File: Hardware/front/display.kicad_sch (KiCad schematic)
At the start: 8 parts

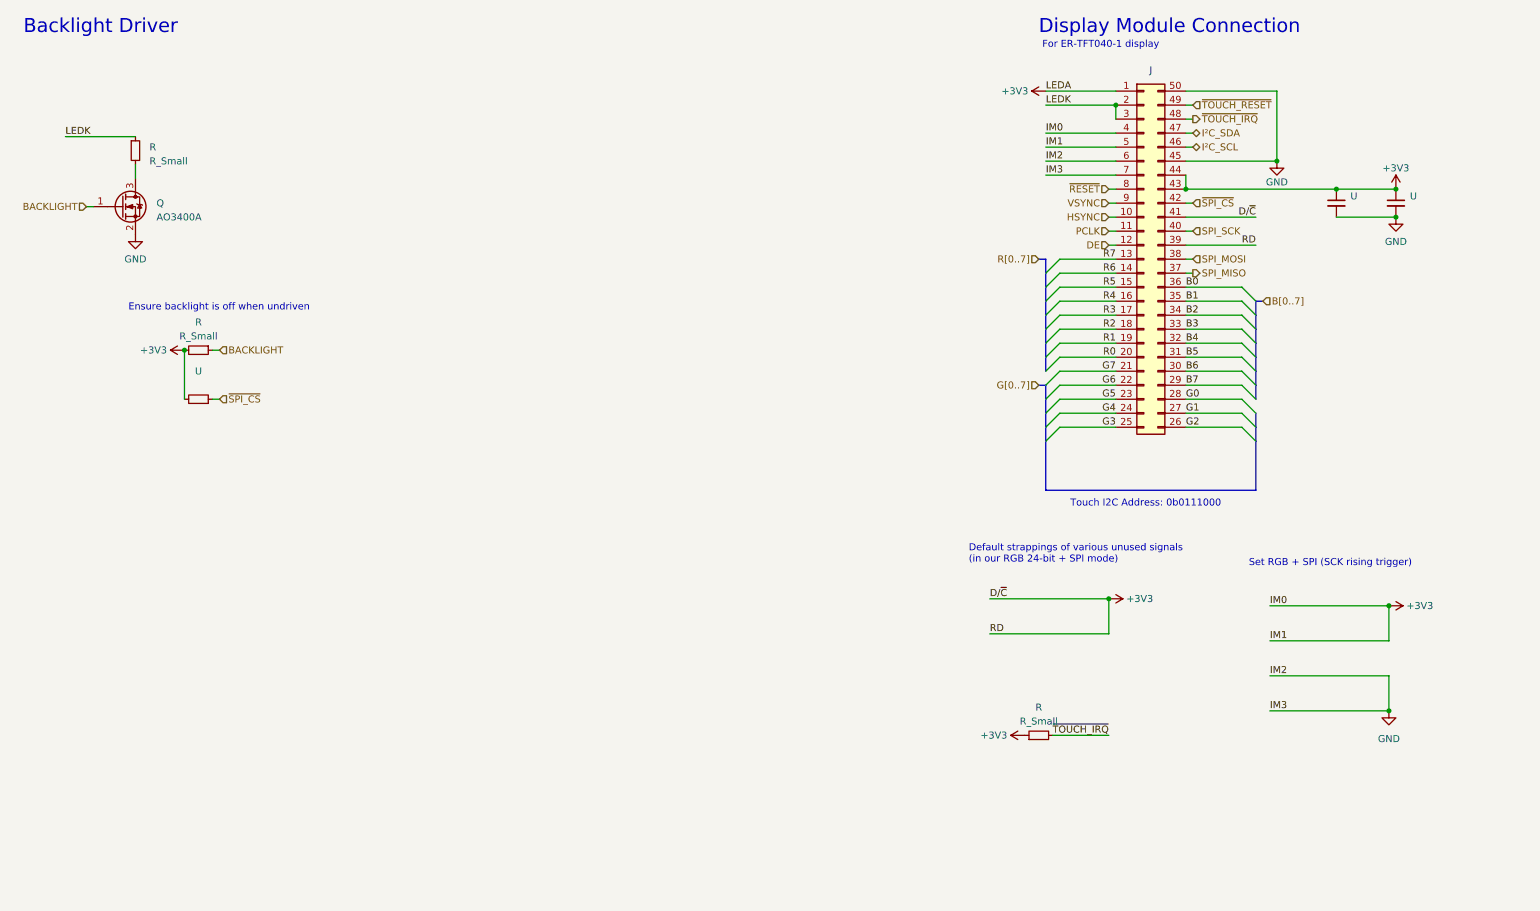
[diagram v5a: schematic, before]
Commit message: hw: First pass at new front panel
- Finished routing all signals on the front panel

- Put back the LED controller (PCA9955B) since that's a very nice and
  convenient way to drive the LEDs; it's driven via a "private" I2C bus
  from the RP2040 instead of the host controlling it.

  The touch panel controller is also hanging off this private bus so we
  can deal with it.

- Made trigger LED bicolor (green/orange)
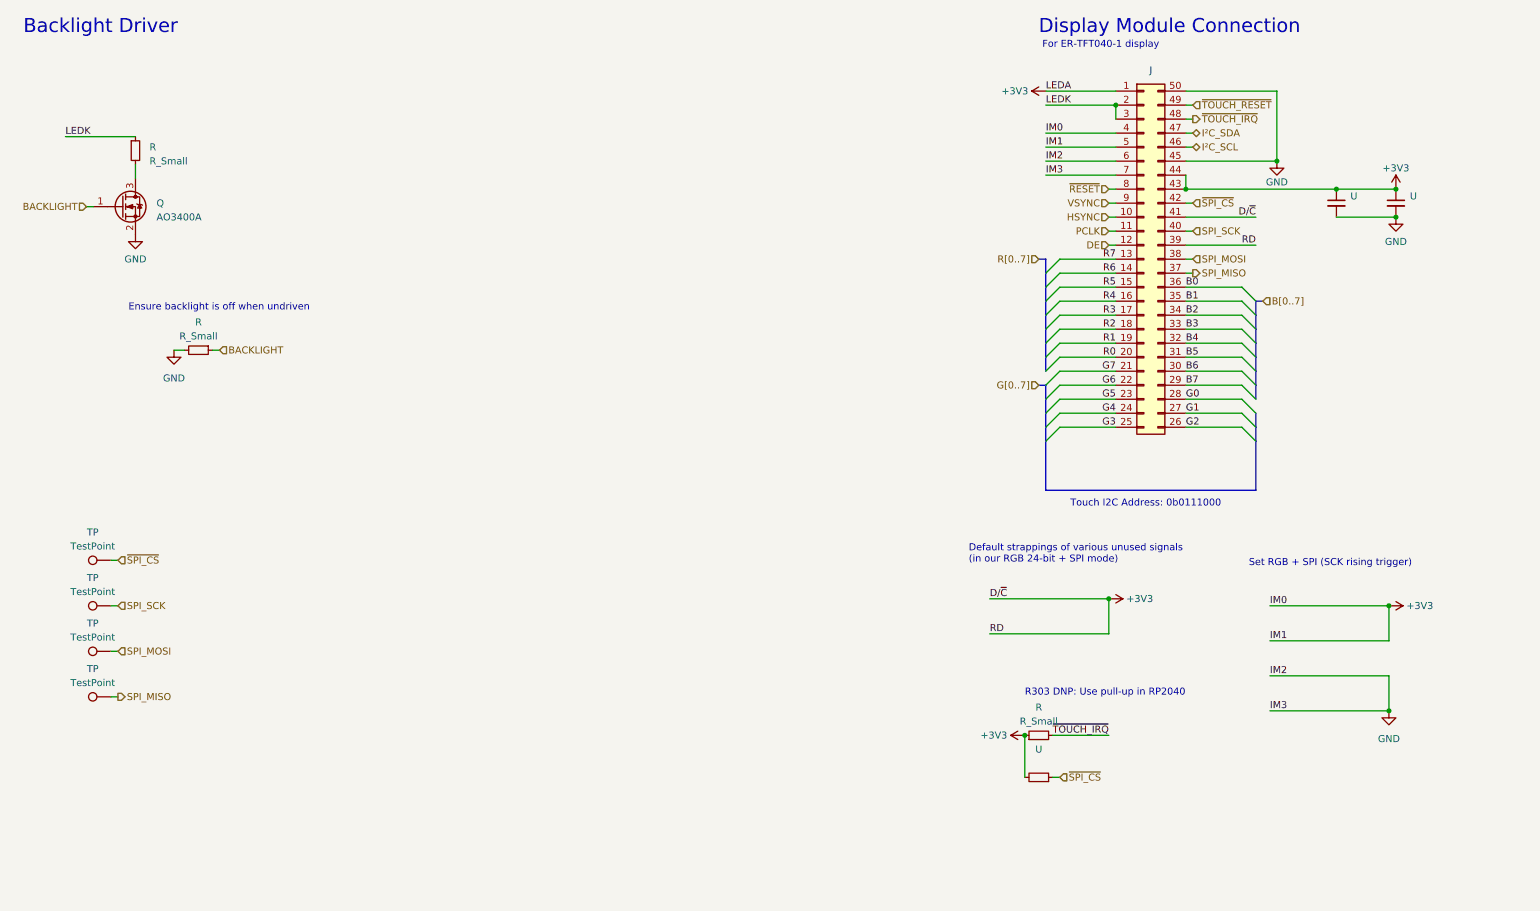
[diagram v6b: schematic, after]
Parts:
- added TP (x4): TestPoint, symbol Connector:TestPoint
- R: now left out of the parts list
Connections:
- net +3V3: no longer R.2
- net GND: now also R.2
- net SPI_MISO: now also TP.1
- net SPI_MOSI: now also TP.1
- net SPI_SCK: now also TP.1
- net ~{SPI_CS}: now also TP.1
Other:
- note added: "R303 DNP: Use pull-up in RP2040"
- moved on the sheet: U
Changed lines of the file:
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@@
   (junction (at 267.97 52.07) (diameter 0) (color 0 0 0 0)
   )
-  (junction (at 48.26 76.2) (diameter 0) (color 0 0 0 0)
+  (junction (at 200.66 146.05) (diameter 0) (color 0 0 0 0)
   )
   (junction (at 266.7 141.605) (diameter 0) (color 0 0 0 0)
@@
     (stroke (width 0) (type default))
   )
+  (wire (pts (xy 46.355 76.2) (xy 48.26 76.2))
+    (stroke (width 0) (type default))
+  )
   (bus (pts (xy 242.57 92.71) (xy 242.57 101.6))
     (stroke (width 0) (type default))
@@
     (stroke (width 0) (type default))
   )
-  (wire (pts (xy 48.26 76.2) (xy 48.26 85.09))
-    (stroke (width 0) (type default))
-  )
   (wire (pts (xy 217.17 31.75) (xy 217.17 34.29))
     (stroke (width 0) (type default))
@@
     (stroke (width 0) (type default))
   )
+  (wire (pts (xy 34.925 130.81) (xy 36.195 130.81))
+    (stroke (width 0) (type default))
+  )
   (bus (pts (xy 204.47 62.23) (xy 204.47 64.77))
     (stroke (width 0) (type default))
@@
     (stroke (width 0) (type default))
   )
+  (wire (pts (xy 34.925 139.065) (xy 36.195 139.065))
+    (stroke (width 0) (type default))
+  )
   (wire (pts (xy 194.31 121.285) (xy 215.9 121.285))
     (stroke (width 0) (type default))
@@
     (stroke (width 0) (type default))
   )
-  (wire (pts (xy 53.34 85.09) (xy 54.61 85.09))
+  (wire (pts (xy 205.74 153.67) (xy 207.01 153.67))
     (stroke (width 0) (type default))
   )
@@
     (stroke (width 0) (type default))
   )
+  (wire (pts (xy 34.925 122.555) (xy 36.195 122.555))
+    (stroke (width 0) (type default))
+  )
   (wire (pts (xy 215.9 52.07) (xy 217.17 52.07))
     (stroke (width 0) (type default))
   )
+  (wire (pts (xy 34.925 114.3) (xy 36.195 114.3))
+    (stroke (width 0) (type default))
+  )
   (bus (pts (xy 204.47 74.93) (xy 204.47 77.47))
     (stroke (width 0) (type default))
@@
     (stroke (width 0) (type default))
   )
+  (wire (pts (xy 200.66 146.05) (xy 200.66 153.67))
+    (stroke (width 0) (type default))
+  )
   (bus (pts (xy 242.57 67.31) (xy 243.84 67.31))
     (stroke (width 0) (type default))
@@
   )
   (text "For ER-TFT040-1 display" (at 203.835 21.59 0)
+    (effects (font (size 1.27 1.27)) (justify left bottom))
+  )
+  (text "R303 DNP: Use pull-up in RP2040" (at 200.66 139.065 0)
     (effects (font (size 1.27 1.27)) (justify left bottom))
   )
@@
     (effects (font (size 1.27 1.27)) (justify right))
   )
+  (hierarchical_label "~{SPI_CS}" (shape input) (at 36.195 114.3 0) (fields_autoplaced)
+    (effects (font (size 1.27 1.27)) (justify left))
+  )
+  (hierarchical_label "SPI_MISO" (shape output) (at 36.195 139.065 0) (fields_autoplaced)
+    (effects (font (size 1.27 1.27)) (justify left))
+  )
   (hierarchical_label "~{TOUCH_IRQ}" (shape output) (at 231.14 34.29 0) (fields_autoplaced)
     (effects (font (size 1.27 1.27)) (justify left))
   )
   (hierarchical_label "BACKLIGHT" (shape input) (at 54.61 76.2 0) (fields_autoplaced)
+    (effects (font (size 1.27 1.27)) (justify left))
+  )
+  (hierarchical_label "SPI_MOSI" (shape input) (at 36.195 130.81 0) (fields_autoplaced)
     (effects (font (size 1.27 1.27)) (justify left))
   )
@@
     (effects (font (size 1.27 1.27)) (justify left))
   )
+  (hierarchical_label "SPI_SCK" (shape input) (at 36.195 122.555 0) (fields_autoplaced)
+    (effects (font (size 1.27 1.27)) (justify left))
+  )
   (hierarchical_label "~{SPI_CS}" (shape input) (at 231.14 49.53 0) (fields_autoplaced)
     (effects (font (size 1.27 1.27)) (justify left))
@@
     (effects (font (size 1.27 1.27)) (justify left))
   )
-  (hierarchical_label "~{SPI_CS}" (shape input) (at 54.61 85.09 0) (fields_autoplaced)
+  (hierarchical_label "~{SPI_CS}" (shape input) (at 207.01 153.67 0) (fields_autoplaced)
     (effects (font (size 1.27 1.27)) (justify left))
   )
   (symbol (lib_id "Device:R_Small") (at 203.2 146.05 90) (unit 1)
-    (in_bom yes) (on_board yes) (fields_autoplaced)
+    (in_bom no) (on_board no) (fields_autoplaced)
     (default_instance (reference "R") (unit 1) (value "R_Small") (footprint ""))
     (property "Reference" "R" (id 0) (at 203.2 140.97 90)
@@
     (pin "1")
   )
+  (symbol (lib_id "Connector:TestPoint") (at 34.925 139.065 90) (unit 1)
+    (in_bom no) (on_board yes) (fields_autoplaced)
+    (default_instance (reference "TP") (unit 1) (value "TestPoint") (footprint ""))
+    (property "Reference" "TP" (id 0) (at 31.623 133.985 90)
+      (effects (font (size 1.27 1.27)))
+    )
+    (property "Value" "TestPoint" (id 1) (at 31.623 136.525 90)
+      (effects (font (size 1.27 1.27)))
+    )
+    (property "Footprint" "" (id 2) (at 34.925 133.985 0)
+      (effects (font (size 1.27 1.27)) hide)
+    )
+    (property "Datasheet" "~" (id 3) (at 34.925 133.985 0)
+      (effects (font (size 1.27 1.27)) hide)
+    )
+    (pin "1")
+  )
   (symbol (lib_id "power:+3V3") (at 215.9 121.285 270) (unit 1)
     (in_bom yes) (on_board yes)
@@
     (pin "1")
   )
-  (symbol (lib_id "Device:R_Small") (at 50.8 85.09 270) (mirror x) (unit 1)
+  (symbol (lib_id "Device:R_Small") (at 203.2 153.67 270) (mirror x) (unit 1)
     (in_bom yes) (on_board yes)
     (default_instance (reference "U") (unit 1) (value "") (footprint ""))
-    (property "Reference" "U" (id 0) (at 50.8 80.01 90)
-      (effects (font (size 1.27 1.27)))
-    )
-    (property "Value" "" (id 1) (at 50.8 82.55 90)
-      (effects (font (size 1.27 1.27)))
-    )
-    (property "Footprint" "" (id 2) (at 50.8 85.09 0)
-      (effects (font (size 1.27 1.27)) hide)
-    )
-    (property "Datasheet" "~" (id 3) (at 50.8 85.09 0)
-      (effects (font (size 1.27 1.27)) hide)
-    )
-    (property "MPN" "" (id 4) (at 50.8 85.09 90)
+    (property "Reference" "U" (id 0) (at 203.2 148.59 90)
+      (effects (font (size 1.27 1.27)))
+    )
+    (property "Value" "" (id 1) (at 203.2 151.13 90)
+      (effects (font (size 1.27 1.27)))
+    )
+    (property "Footprint" "" (id 2) (at 203.2 153.67 0)
+      (effects (font (size 1.27 1.27)) hide)
+    )
+    (property "Datasheet" "~" (id 3) (at 203.2 153.67 0)
+      (effects (font (size 1.27 1.27)) hide)
+    )
+    (property "MPN" "" (id 4) (at 203.2 153.67 90)
       (effects (font (size 1.27 1.27)) hide)
     )
@@
     (pin "1")
   )
-  (symbol (lib_id "power:+3V3") (at 48.26 76.2 90) (unit 1)
-    (in_bom yes) (on_board yes)
-    (default_instance (reference "#PWR") (unit 1) (value "+3V3") (footprint ""))
-    (property "Reference" "#PWR" (id 0) (at 52.07 76.2 0)
-      (effects (font (size 1.27 1.27)) hide)
-    )
-    (property "Value" "+3V3" (id 1) (at 45.085 76.2 90)
-      (effects (font (size 1.27 1.27)) (justify left))
-    )
-    (property "Footprint" "" (id 2) (at 48.26 76.2 0)
-      (effects (font (size 1.27 1.27)) hide)
-    )
-    (property "Datasheet" "" (id 3) (at 48.26 76.2 0)
+  (symbol (lib_id "Connector:TestPoint") (at 34.925 122.555 90) (unit 1)
+    (in_bom no) (on_board yes) (fields_autoplaced)
+    (default_instance (reference "TP") (unit 1) (value "TestPoint") (footprint ""))
+    (property "Reference" "TP" (id 0) (at 31.623 117.475 90)
+      (effects (font (size 1.27 1.27)))
+    )
+    (property "Value" "TestPoint" (id 1) (at 31.623 120.015 90)
+      (effects (font (size 1.27 1.27)))
+    )
+    (property "Footprint" "" (id 2) (at 34.925 117.475 0)
+      (effects (font (size 1.27 1.27)) hide)
+    )
+    (property "Datasheet" "~" (id 3) (at 34.925 117.475 0)
       (effects (font (size 1.27 1.27)) hide)
     )
@@
     (pin "2")
   )
+  (symbol (lib_id "Connector:TestPoint") (at 34.925 130.81 90) (unit 1)
+    (in_bom no) (on_board yes) (fields_autoplaced)
+    (default_instance (reference "TP") (unit 1) (value "TestPoint") (footprint ""))
+    (property "Reference" "TP" (id 0) (at 31.623 125.73 90)
+      (effects (font (size 1.27 1.27)))
+    )
+    (property "Value" "TestPoint" (id 1) (at 31.623 128.27 90)
+      (effects (font (size 1.27 1.27)))
+    )
+    (property "Footprint" "" (id 2) (at 34.925 125.73 0)
+      (effects (font (size 1.27 1.27)) hide)
+    )
+    (property "Datasheet" "~" (id 3) (at 34.925 125.73 0)
+      (effects (font (size 1.27 1.27)) hide)
+    )
+    (pin "1")
+  )
   (symbol (lib_id "Device:R_Small") (at 39.37 40.005 0) (unit 1)
     (in_bom yes) (on_board yes) (fields_autoplaced)
@@
     )
     (property "Datasheet" "" (id 3) (at 267.97 52.07 0)
+      (effects (font (size 1.27 1.27)) hide)
+    )
+    (pin "1")
+  )
+  (symbol (lib_id "power:GND") (at 46.355 76.2 0) (unit 1)
+    (in_bom yes) (on_board yes) (fields_autoplaced)
+    (default_instance (reference "#PWR") (unit 1) (value "GND") (footprint ""))
+    (property "Reference" "#PWR" (id 0) (at 46.355 82.55 0)
+      (effects (font (size 1.27 1.27)) hide)
+    )
+    (property "Value" "GND" (id 1) (at 46.355 81.28 0)
+      (effects (font (size 1.27 1.27)))
+    )
+    (property "Footprint" "" (id 2) (at 46.355 76.2 0)
+      (effects (font (size 1.27 1.27)) hide)
+    )
+    (property "Datasheet" "" (id 3) (at 46.355 76.2 0)
       (effects (font (size 1.27 1.27)) hide)
     )
@@
     (pin "2")
   )
+  (symbol (lib_id "Connector:TestPoint") (at 34.925 114.3 90) (unit 1)
+    (in_bom no) (on_board yes) (fields_autoplaced)
+    (default_instance (reference "TP") (unit 1) (value "TestPoint") (footprint ""))
+    (property "Reference" "TP" (id 0) (at 31.623 109.22 90)
+      (effects (font (size 1.27 1.27)))
+    )
+    (property "Value" "TestPoint" (id 1) (at 31.623 111.76 90)
+      (effects (font (size 1.27 1.27)))
+    )
+    (property "Footprint" "" (id 2) (at 34.925 109.22 0)
+      (effects (font (size 1.27 1.27)) hide)
+    )
+    (property "Datasheet" "~" (id 3) (at 34.925 109.22 0)
+      (effects (font (size 1.27 1.27)) hide)
+    )
+    (pin "1")
+  )
   (symbol (lib_id "power:GND") (at 266.7 141.605 0) (unit 1)
